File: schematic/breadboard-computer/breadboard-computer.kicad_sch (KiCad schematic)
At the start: 7 parts, among them U1 NE555P

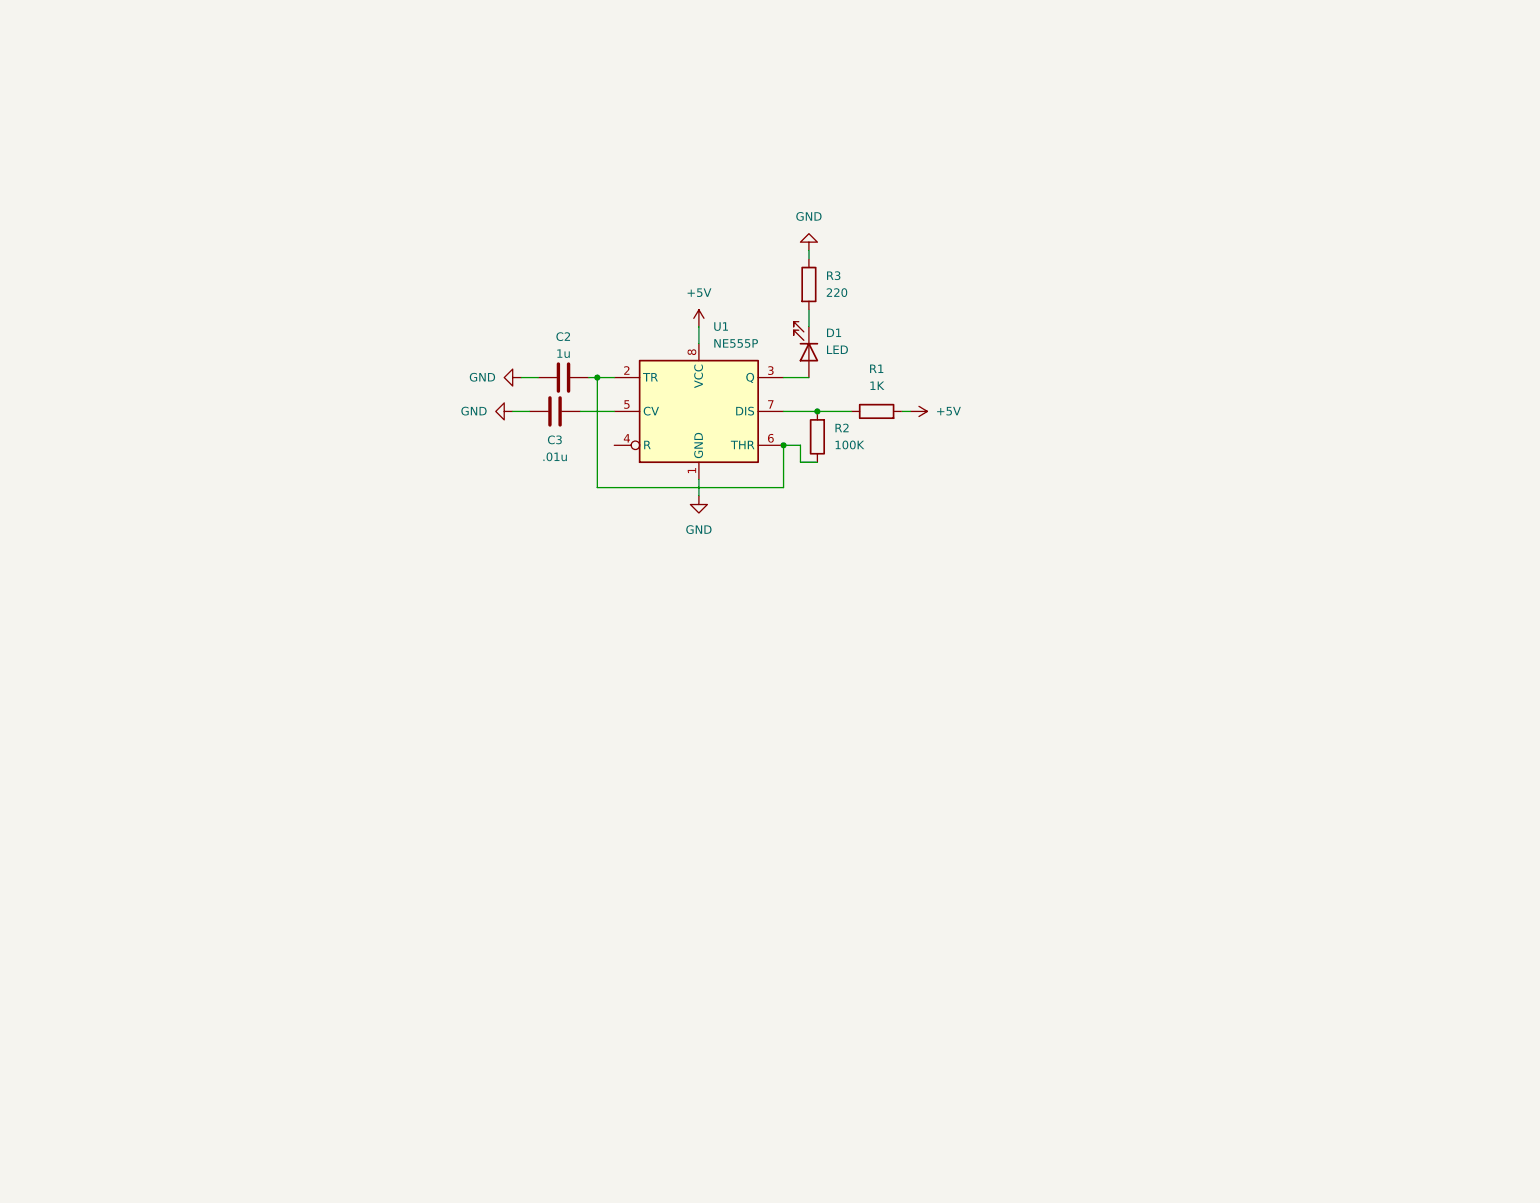
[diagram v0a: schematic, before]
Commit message: Updated clock module schematic, added picture
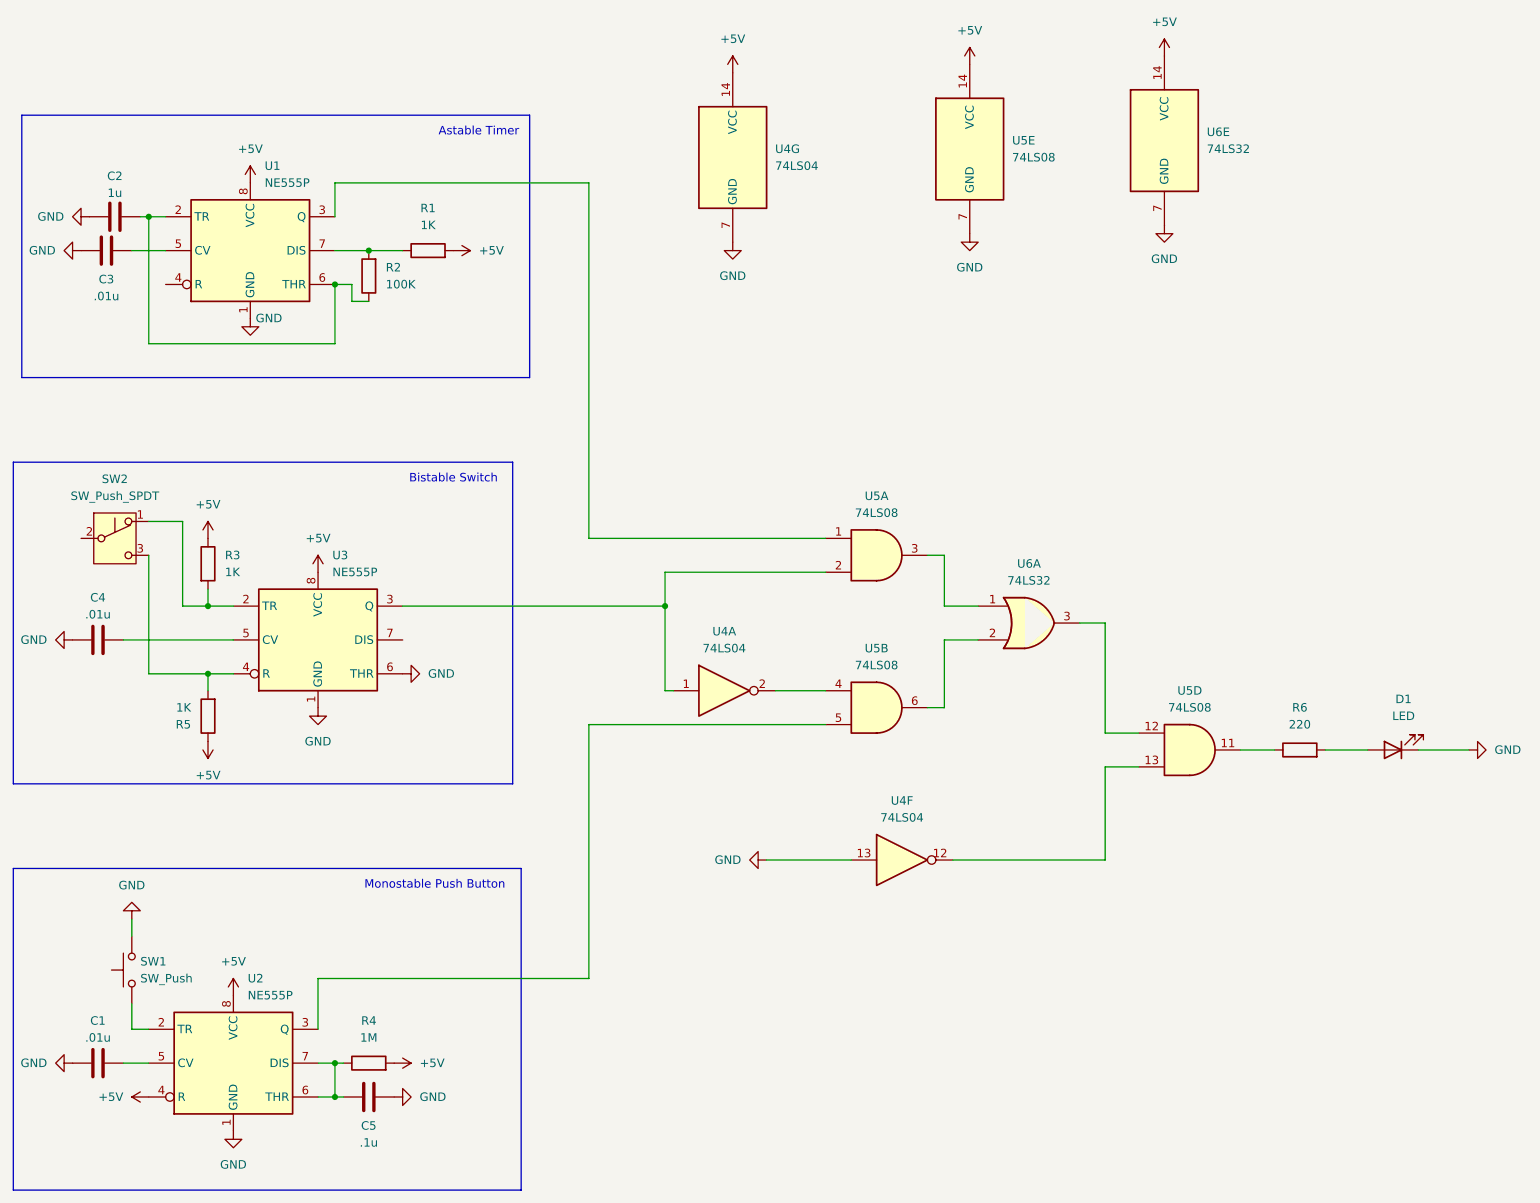
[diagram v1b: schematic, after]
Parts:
- added C1, C4: .01u, symbol Device:C
- added C5: .1u, symbol Device:C
- added R4: 1M, symbol Device:R
- added R5: 1K, symbol Device:R
- added R6: 220, symbol Device:R
- added SW1: SW_Push, symbol Switch:SW_Push
- added SW2: SW_Push_SPDT, symbol Switch:SW_Push_SPDT
- added U2, U3: NE555P, Package_DIP:DIP-8_W7.62mm, symbol Timer:NE555P
- added U4: 74LS04, symbol 74xx:74LS04
- added U5: 74LS08, symbol 74xx:74LS08
- added U6: 74LS32, symbol 74xx:74LS32
- R3: value 220 -> 1K
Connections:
- net +5V: now also R3.1, R4.2, R5.1, U2.4 (R), U2.8 (VCC), U3.8 (VCC), U4.14 (VCC), U5.14 (VCC), U6.14 (VCC)
- net GND: now also D1.1 (K), C1.1, C4.1, C5.2, SW1.2, U2.1 (GND), U3.1 (GND), U3.6 (THR), U4.13, U4.7 (GND), U5.7 (GND), U6.7 (GND); no longer R3.1
- net at R3.2: now also SW2.1 (A), U3.2 (TR); no longer D1.1 (K)
- net at D1.2 (A): now also R6.2; no longer U1.3 (Q)
- new net: U3.3 (Q), U4.1, U5.2
- new net: U4.2, U5.4
- new net: C5.1, R4.1, U2.6 (THR), U2.7 (DIS)
- new net: SW1.1, U2.2 (TR)
- new net: U2.3 (Q), U5.5
- new net: C1.2, U2.5 (CV)
- new net: R6.1, U5.11
- new net: U5.12, U6.3
- new net: U4.12, U5.13
- new net: U5.6, U6.2
- new net: R5.2, SW2.3 (C), U3.4 (R)
- new net: U1.3 (Q), U5.1
- new net: U5.3, U6.1
- new net: C4.2, U3.5 (CV)
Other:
- note added: "Astable Timer"
- note added: "Bistable Switch"
- note added: "Monostable Push Button"
- moved on the sheet: C2, C3, R1, R2, U1
